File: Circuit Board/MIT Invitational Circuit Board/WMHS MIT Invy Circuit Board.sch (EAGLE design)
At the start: 361 parts, among them IC1101 7805DT, IC1201 7805DT, IC1301 7805DT, IC1501 7805DT, J1005 ICSP_HEADER, J1104 ICSP_HEADER, J1204 ICSP_HEADER, J1304 ICSP_HEADER, J204 ICSP_HEADER, J301 ICSP_HEADER, J401 ICSP_HEADER, J503 ICSP_HEADER, J603 ICSP_HEADER, J703 ICSP_HEADER, J704 ICSP_HEADER, J903 ICSP_HEADER, Q1001 PSMN7R0-60YS, Q1401 PSMN7R0-60YS, Q201 PSMN7R0-60YS, Q301 500mA/300V, Q401 500mA/300V, Q501 PSMN7R0-60YS, Q601 PSMN7R0-60YS, Q801 PSMN7R0-60YS, Q901 PSMN7R0-60YS, U1001 ATTINY25-20SSUR, U1002 MIC5205, U101 74HC1G04, U102 MIC5205, U1101 DRV8835, U1102 ATTINY25-20SSUR, U1201 DRV8835, U1202 ATTINY25-20SSUR, U1301 DRV8835, U1302 ATTINY25-20SSUR, U1401 74HC1G04, U1402 MIC5205, U201 74HC1G04, U202 ATTINY25-20SSUR, U203 MIC5205, U301 74HC1G04, U302 SN74C1G08-DCK, U303 ATTINY25-20SSUR, U304 MIC5205, U401 74HC1G04, U402 SN74C1G08-DCK, U403 ATTINY25-20SSUR, U404 MIC5205, U501 74HC1G04, U502 SN74C1G08-DCK, U503 ATTINY25-20SSUR, U504 MIC5205, U601 74HC1G04, U602 SN74C1G08-DCK, U603 ATTINY25-20SSUR, U604 MIC5205, U701 ATTINY25-20SSUR, U702 ATTINY25-20SSUR, U703 MIC5205, U801 74HC1G04, U802 SN74C1G08-DCK, U803 MIC5205, U901 ATTINY25-20SSUR, U902 MIC5205, X1601 MSTBA2

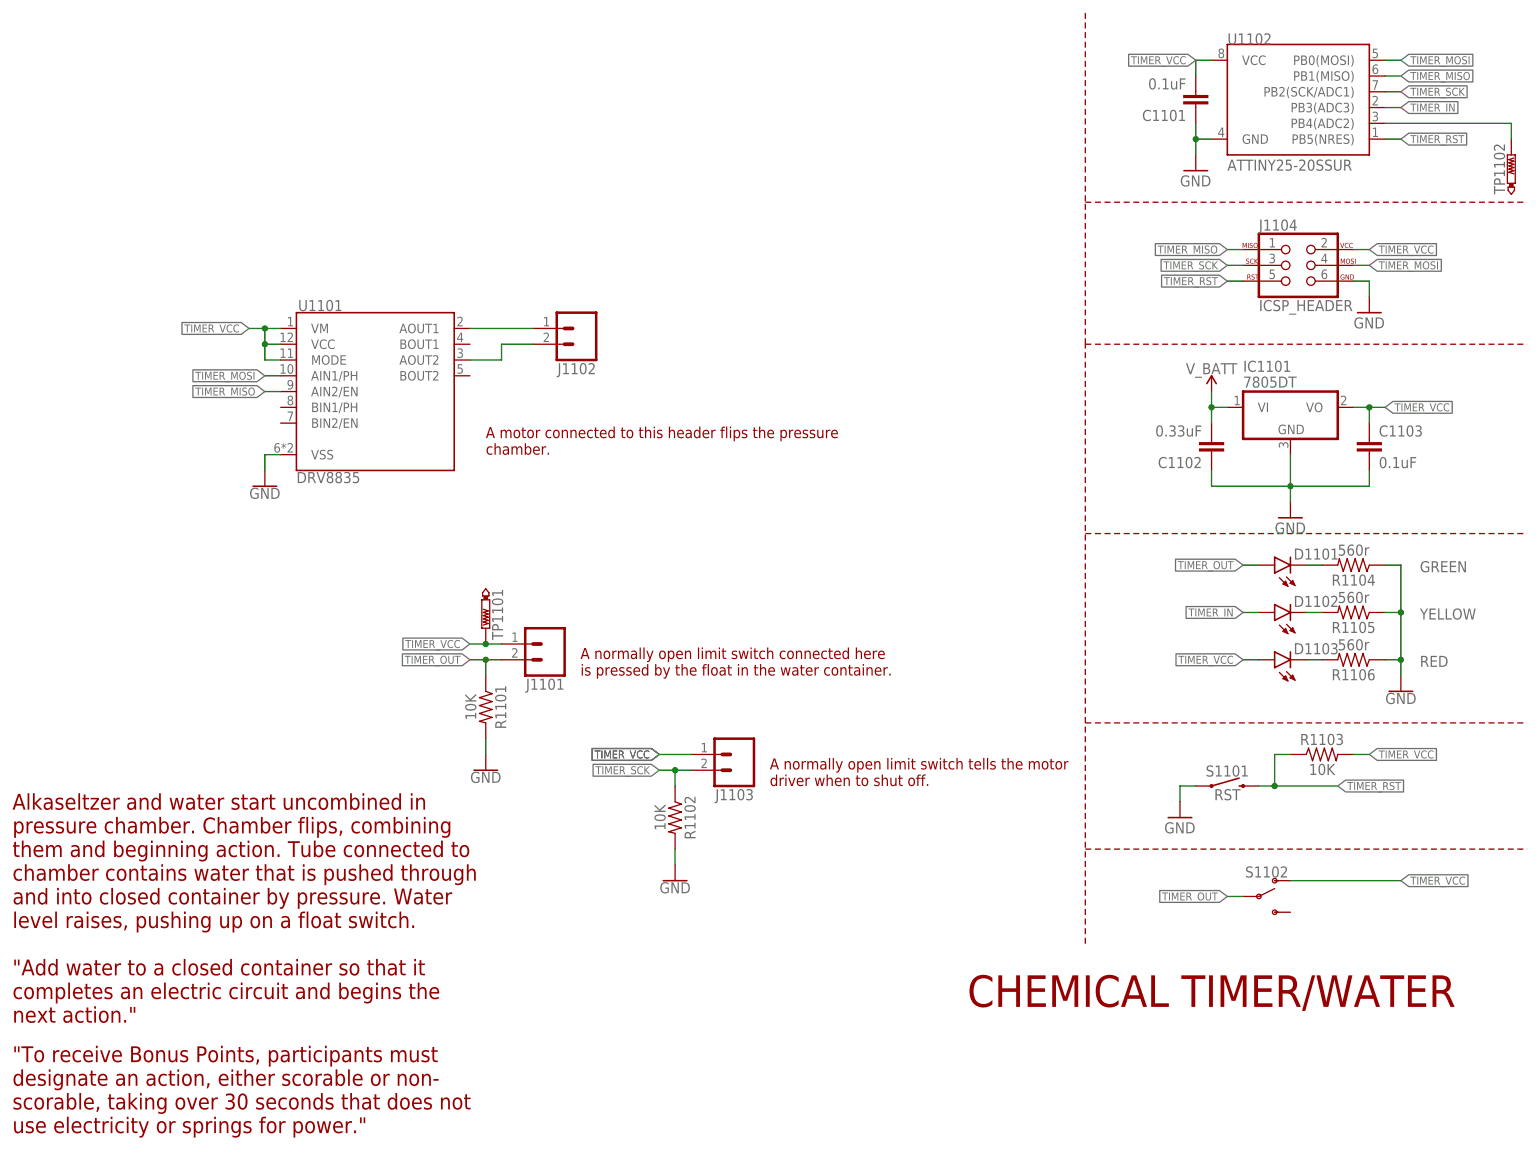
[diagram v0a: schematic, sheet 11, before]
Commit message: Changed file naming system
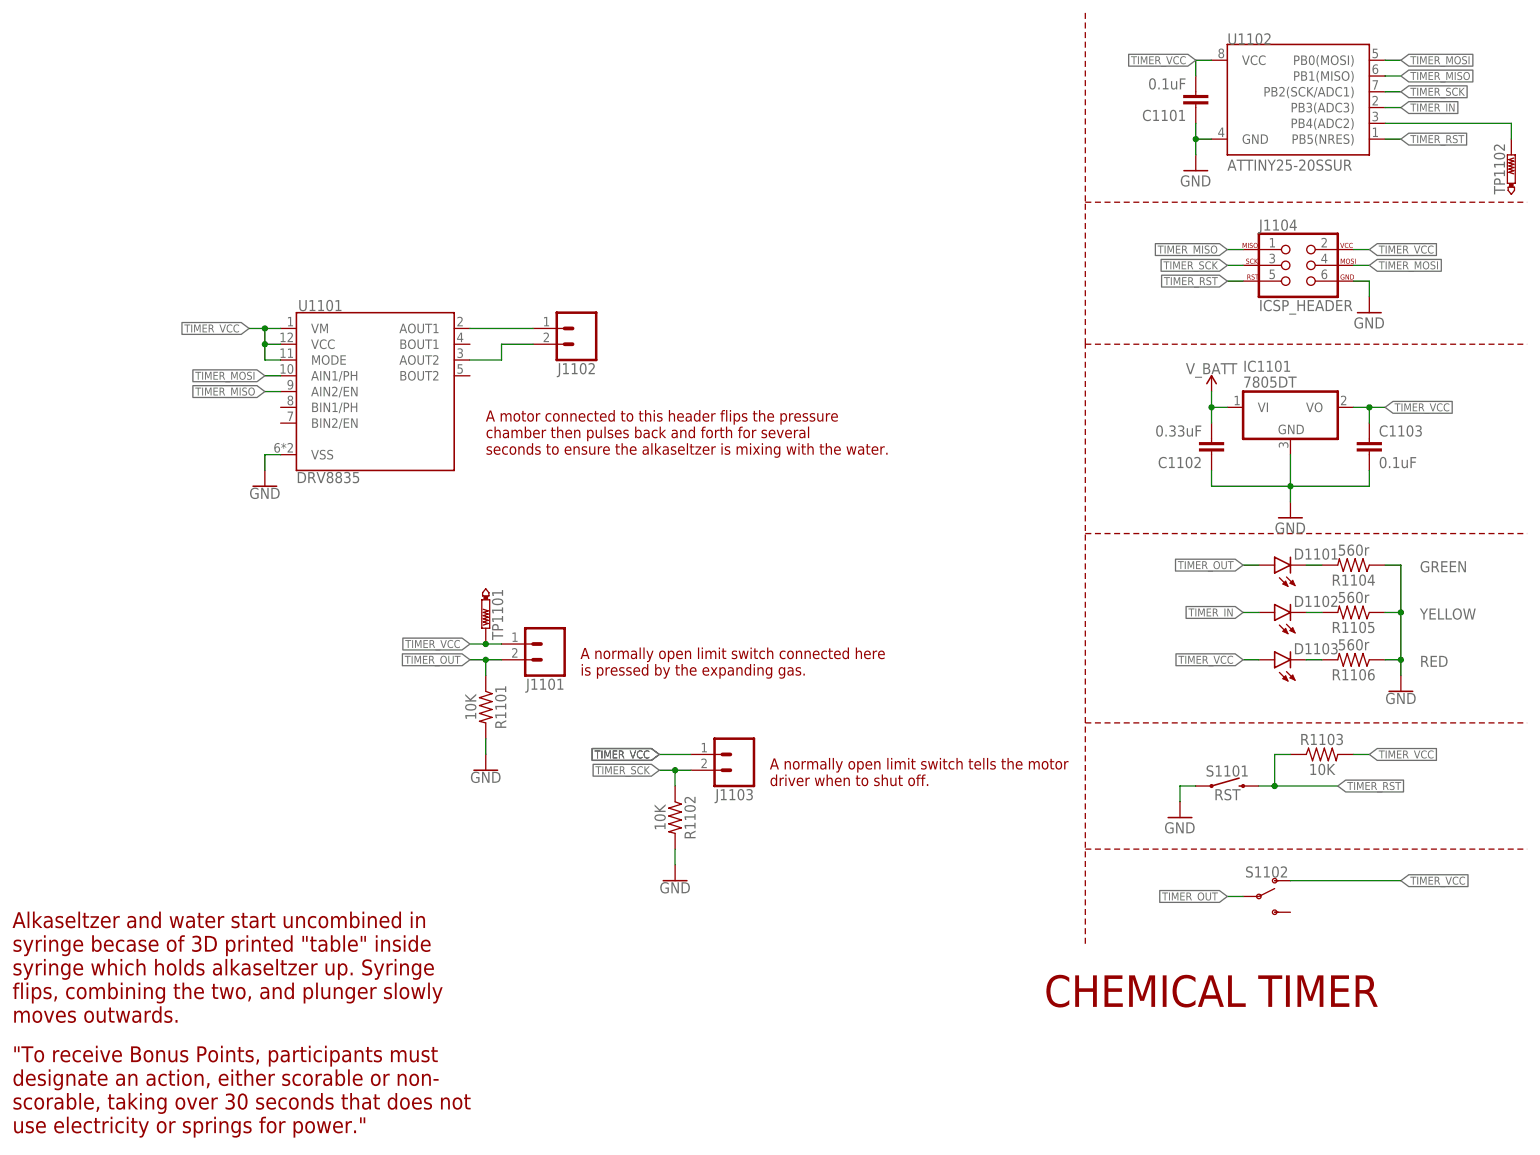
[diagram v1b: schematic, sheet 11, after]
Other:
- note added: "A motor connected to this header flips the pressure chamber then pulses back and forth for several seconds to ensure the alkaseltzer is mixing with the water."
- note added: "A normally open limit switch connected here is pressed by the expanding gas."
- note added: "A set of probes is connected to this header. When salt water from the capillary tube bridges between the electrodes, the next action's microcontroller picks up the change and begins the next action. Bypassed at MIT; instead arduino pro mini was used to read and send signal to next action."
- note added: "A solenoid valve is connected to J502. A mosfet attached to the microcontroller controlls the state of the valve."
- note added: "A solenoid valve is opened, releasing water into a test tube containing ammonium nitrate powder. The powder dissolves in an endothermic reaction, causing the resistance of a thermistor to change."
- note added: "A solenoid valve opens, releasing a small amount of fresh water into a test tube already containing salt water. The salt water level raises, touching two electrodes. The change in resistance is sensed by the microcontroller, which begins the next action."
- note added: "A thermistor is used to check the temperature of the reaction."
- note added: "Alkaseltzer and water start uncombined in syringe becase of 3D printed "table" inside syringe which holds alkaseltzer up. Syringe flips, combining the two, and plunger slowly moves outwards."
- note added: "An optional 12V brushless fan can be connected to J5 in order to cool the interface between the heater and the device. Used to power external arduino pro mini because of unreliable timer microcontroller at MIT."
- note added: "CHEMICAL TIMER"
- note added: "Syringe with baking soda filled basket attached to plunger is filled with 30% warm vinegar. When syringe is flipped, the two react and the resulting reaction inflates a balloon which hits a limit switch 20cm away."
- note removed: "A motor connected to this header flips the pressure chamber."
- note removed: "A normally open limit switch connected here is pressed by the float in the water container."
- note removed: "A set of probes is connected to this header. When salt water from the capillary tube bridges between the electrodes, the next action's microcontroller picks up the change and begins the next action."
- note removed: "A solenoid dunks a thermistor into a container of ice water. The endothermic action of heat being transferred from the thermistor casing to the water is detected by the microcontroller which begins the next action."
- note removed: "A solenoid is connected to J502. A mosfet attached to the microcontroller controls it."
- note removed: "A thermistor is monitored continuously to detect when the endothermic action happens."
- note removed: "Alkaseltzer and water start uncombined in pressure chamber. Chamber flips, combining them and beginning action. Tube connected to chamber contains water that is pushed through and into closed container by pressure. Water level raises, pushing up on a float switch."
- note removed: "An optional 12V brushless fan can be connected to J5 in order to cool the interface between the heater and the device."
- note removed: "CHEMICAL TIMER/WATER"
- note removed: "Pressure chamber with baking soda and 30% warm vinegar is flipped, the two react and the resulting reaction inflates a balloon which hits a limit switch 20cm away."
- note removed: "Update 1/22/2018: Action has been combined with timer action. New action is better suited to the electronics available on the timer section, so none of these components are being used and the transfer will be bypassed via jumpers."
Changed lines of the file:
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@@
 next action as a result of the reduction in
 temperature."</text>
-<text x="91.44" y="58.42" size="1.778" layer="94">A thermistor is monitored continuously to
-detect when the endothermic action happens.</text>
-<text x="106.68" y="129.54" size="1.778" layer="94">A solenoid is connected to J502. A mosfet
-attached to the microcontroller controls it.</text>
+<text x="91.44" y="58.42" size="1.778" layer="94">A thermistor is used to check
+the temperature of the reaction.</text>
+<text x="106.68" y="129.54" size="1.778" layer="94">A solenoid valve is connected to J502. A mosfet
+attached to the microcontroller controlls the
+state of the valve.</text>
 <wire x1="177.8" y1="185.42" x2="177.8" y2="152.4" width="0.1524" layer="94" style="dashdot"/>
 <wire x1="177.8" y1="152.4" x2="248.92" y2="152.4" width="0.1524" layer="94" style="longdash"/>
@@
 <wire x1="177.8" y1="50.8" x2="248.92" y2="50.8" width="0.1524" layer="94" style="longdash"/>
 <wire x1="177.8" y1="35.56" x2="177.8" y2="152.4" width="0.1524" layer="94" style="dashdot"/>
-<text x="5.08" y="17.78" size="2.54" layer="94">A solenoid dunks a thermistor into a container
-of ice water. The endothermic action of heat
-being transferred from the thermistor casing to
-the water is detected by the microcontroller
-which begins the next action.</text>
+<text x="5.08" y="17.78" size="2.54" layer="94">A solenoid valve is opened, releasing water
+into a test tube containing ammonium nitrate
+powder. The powder dissolves in an
+endothermic reaction, causing the resistance
+of a thermistor to change.</text>
 <text x="91.44" y="43.18" size="1.778" layer="98">Revision Jan 2018: Add 10K resistor to
 back of PCB between ICSP pins SCK and VCC
@@
 <plain>
 <text x="195.58" y="27.94" size="5.08" layer="94" align="center">WATER ACTION</text>
+<text x="5.08" y="5.08" size="2.54" layer="94">"Add water to a closed container so that it
+completes an electric circuit and begins the
+next action."</text>
 <text x="119.38" y="134.62" size="1.778" layer="94">A solenoid valve is connected here. A mosfet
 attached to the microcontroller controls the
@@
 <wire x1="177.8" y1="50.8" x2="248.92" y2="50.8" width="0.1524" layer="94" style="longdash"/>
 <wire x1="177.8" y1="35.56" x2="177.8" y2="152.4" width="0.1524" layer="94" style="dashdot"/>
-<wire x1="12.7" y1="154.94" x2="12.7" y2="63.5" width="0.1524" layer="98" style="shortdash"/>
-<wire x1="246.38" y1="38.1" x2="246.38" y2="180.34" width="0.1524" layer="98" style="shortdash"/>
-<text x="15.24" y="160.02" size="1.778" layer="98">Update 1/22/2018: Action has been combined
-with timer action. New action is better suited to
-the electronics available on the timer section,
-so none of these components are being used
-and the transfer will be bypassed via jumpers.</text>
-<wire x1="12.7" y1="63.5" x2="175.26" y2="63.5" width="0.1524" layer="98" style="shortdash"/>
-<wire x1="175.26" y1="63.5" x2="175.26" y2="38.1" width="0.1524" layer="98" style="shortdash"/>
-<wire x1="175.26" y1="38.1" x2="246.38" y2="38.1" width="0.1524" layer="98" style="shortdash"/>
-<wire x1="246.38" y1="180.34" x2="165.1" y2="180.34" width="0.1524" layer="98" style="shortdash"/>
-<wire x1="165.1" y1="180.34" x2="165.1" y2="154.94" width="0.1524" layer="98" style="shortdash"/>
-<wire x1="165.1" y1="154.94" x2="83.82" y2="154.94" width="0.1524" layer="98" style="shortdash"/>
-<wire x1="83.82" y1="154.94" x2="12.7" y2="154.94" width="0.1524" layer="98" style="shortdash"/>
-<wire x1="83.82" y1="154.94" x2="83.82" y2="157.48" width="0.1524" layer="98" style="shortdash"/>
-<wire x1="83.82" y1="157.48" x2="76.2" y2="165.1" width="0.1524" layer="98" style="shortdash"/>
-<wire x1="76.2" y1="165.1" x2="68.58" y2="165.1" width="0.1524" layer="98" style="shortdash"/>
+<text x="5.08" y="17.78" size="2.54" layer="94">A solenoid valve opens, releasing a small
+amount of fresh water into a test tube already
+containing salt water. The salt water level
+raises, touching two electrodes. The change in
+resistance is sensed by the microcontroller,
+which begins the next action.</text>
 </plain>
 <instances>
@@
 bridges between the electrodes, the next
 action's microcontroller picks up the change
-and begins the next action.</text>
+and begins the next action. Bypassed at MIT;
+instead arduino pro mini was used to read and
+send signal to next action.</text>
 <text x="68.58" y="78.74" size="1.778" layer="94">A thermistor connected to J39 provides
 feedback for the heater cartridge and is used
@@
 <text x="106.68" y="58.42" size="1.778" layer="94">An optional 12V brushless fan can be
 connected to J5 in order to cool the interface
-between the heater and the device.</text>
+between the heater and the device. Used to
+power external arduino pro mini because of
+unreliable timer microcontroller at MIT.</text>
 <wire x1="177.8" y1="185.42" x2="177.8" y2="152.4" width="0.1524" layer="94" style="dashdot"/>
 <wire x1="177.8" y1="152.4" x2="248.92" y2="152.4" width="0.1524" layer="94" style="longdash"/>
@@
 </sheet>
 <sheet>
-<description>Timer/Water</description>
+<description>Timer</description>
 <plain>
-<text x="198.12" y="27.94" size="5.08" layer="94" align="center">CHEMICAL TIMER/WATER</text>
+<text x="198.12" y="27.94" size="5.08" layer="94" align="center">CHEMICAL TIMER</text>
 <text x="5.08" y="5.08" size="2.54" layer="94">"To receive Bonus Points, participants must
 designate an action, either scorable or non-
@@
 use electricity or springs for power."</text>
 <text x="96.52" y="78.74" size="1.778" layer="94">A normally open limit switch connected here
-is pressed by the float in the water container.</text>
+is pressed by the expanding gas.</text>
 <text x="81.28" y="114.3" size="1.778" layer="94">A motor connected to this header flips the pressure
-chamber.</text>
+chamber then pulses back and forth for several
+seconds to ensure the alkaseltzer is mixing with the water.</text>
 <wire x1="177.8" y1="185.42" x2="177.8" y2="154.94" width="0.1524" layer="94" style="dashdot"/>
 <wire x1="177.8" y1="154.94" x2="248.92" y2="154.94" width="0.1524" layer="94" style="longdash"/>
@@
 <text x="127" y="60.96" size="1.778" layer="94">A normally open limit switch tells the motor
 driver when to shut off.</text>
-<text x="5.08" y="38.1" size="2.54" layer="94">Alkaseltzer and water start uncombined in
-pressure chamber. Chamber flips, combining
-them and beginning action. Tube connected to
-chamber contains water that is pushed through
-and into closed container by pressure. Water
-level raises, pushing up on a float switch.</text>
-<text x="5.08" y="22.86" size="2.54" layer="94">"Add water to a closed container so that it
-completes an electric circuit and begins the
-next action."</text>
+<text x="5.08" y="22.86" size="2.54" layer="94">Alkaseltzer and water start uncombined in
+syringe becase of 3D printed "table" inside
+syringe which holds alkaseltzer up. Syringe
+flips, combining the two, and plunger slowly
+moves outwards.</text>
 </plain>
 <instances>
@@
 <text x="109.22" y="66.04" size="1.778" layer="94">A normally open limit switch tells the motor
 driver when to shut off.</text>
-<text x="5.08" y="25.4" size="2.54" layer="94">Pressure chamber with baking soda and 30%
-warm vinegar is flipped, the two react and the
+<text x="5.08" y="25.4" size="2.54" layer="94">Syringe with baking soda filled basket attached
+to plunger is filled with 30% warm vinegar.
+When syringe is flipped, the two react and the
 resulting reaction inflates a balloon which hits
 a limit switch 20cm away.</text>
